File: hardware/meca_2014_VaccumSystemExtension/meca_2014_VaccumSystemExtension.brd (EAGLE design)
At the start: 45 x 40 mm, 37 parts, among them IC1 ADP3331ARTZ-REEL7, IC2 ADP3331ARTZ-REEL7, IC3 ADP3331ARTZ-REEL7, IC4 ADP3331ARTZ-REEL7

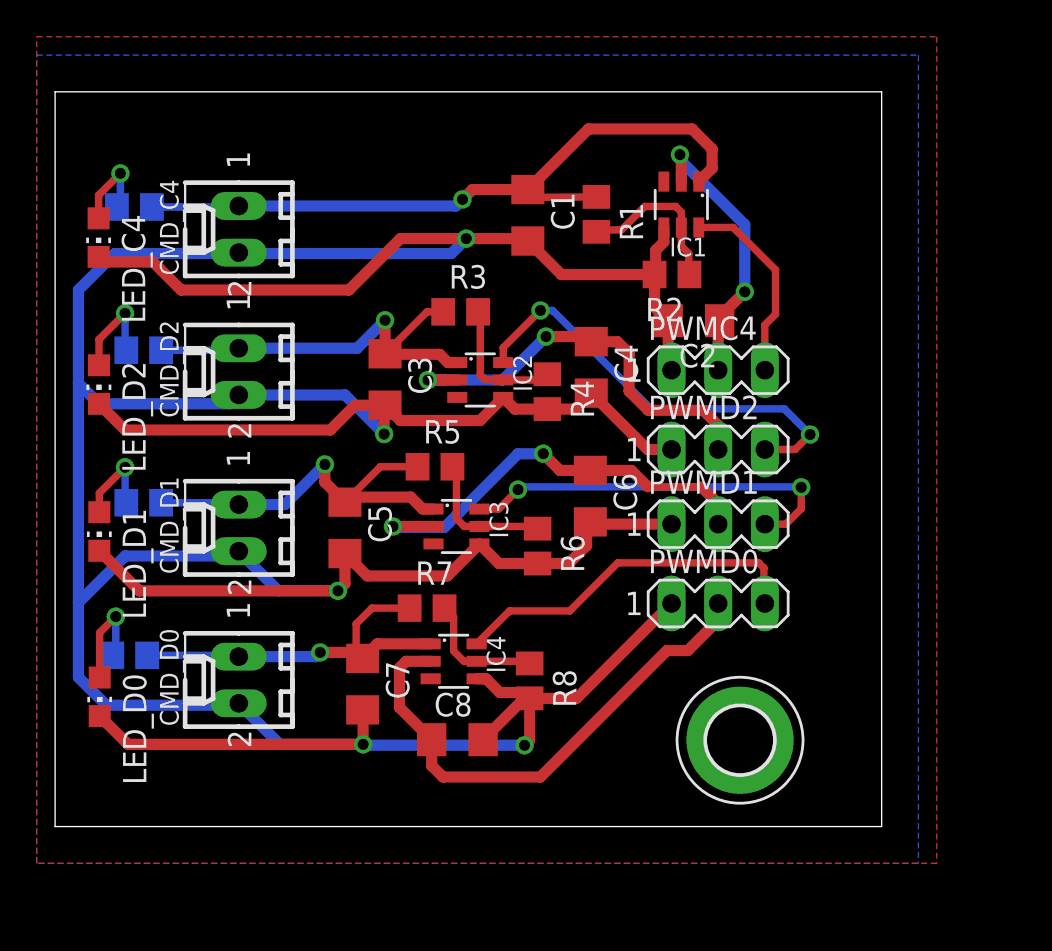
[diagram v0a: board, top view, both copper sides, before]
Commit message: diameter of via increased
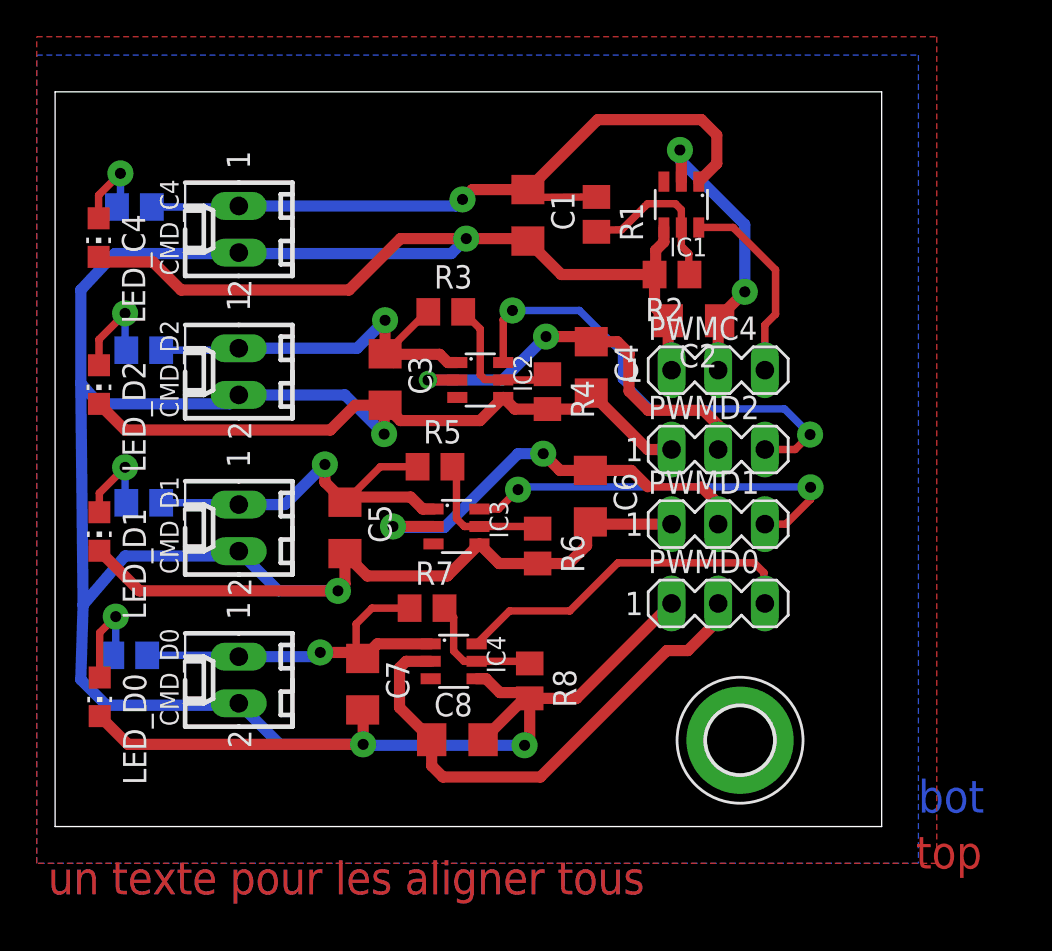
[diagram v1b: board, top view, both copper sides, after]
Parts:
- moved R3 0.81 mm to (21.3, 28.0)
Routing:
- net PWM_D2_5V: track 24.0 -> 25.7 mm
- net N$3: track 38.7 -> 39.9 mm
- net N$6: track 25.0 -> 24.2 mm
- net PWM_D1_5V: track 21.6 -> 22.3 mm
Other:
- board text added: "bot"
- board text added: "top"
- board text added: "un texte pour les aligner tous"
